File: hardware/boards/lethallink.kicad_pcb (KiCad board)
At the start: 6 copper layers, 86 x 111.1 mm, 125 parts, among them J1 PCIe-x4, J2 USB3_Micro_B_Amphenol, Q1 Q_NMOS_GSD, Q2 Q_NMOS_GSD, Q3 Q_NMOS_GSD, Q4 Q_NMOS_GSD, Q5 SI7232DN-T1-GE3, SW1 SW_DIP_x03, U1 ECP5UM5G-381caBGA, U2 ADP5050ACPZ-R7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

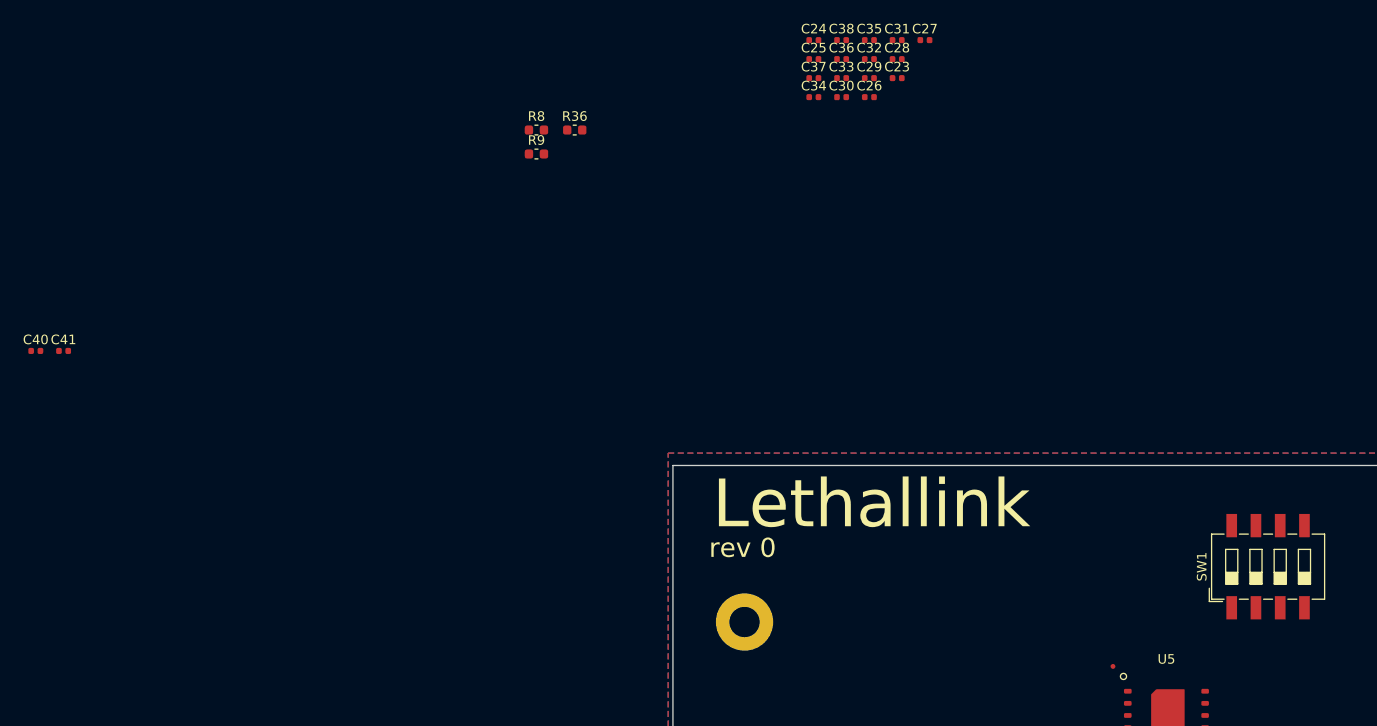
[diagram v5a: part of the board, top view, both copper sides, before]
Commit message: Spent a bit of time putting the unrouted parts back on-grid
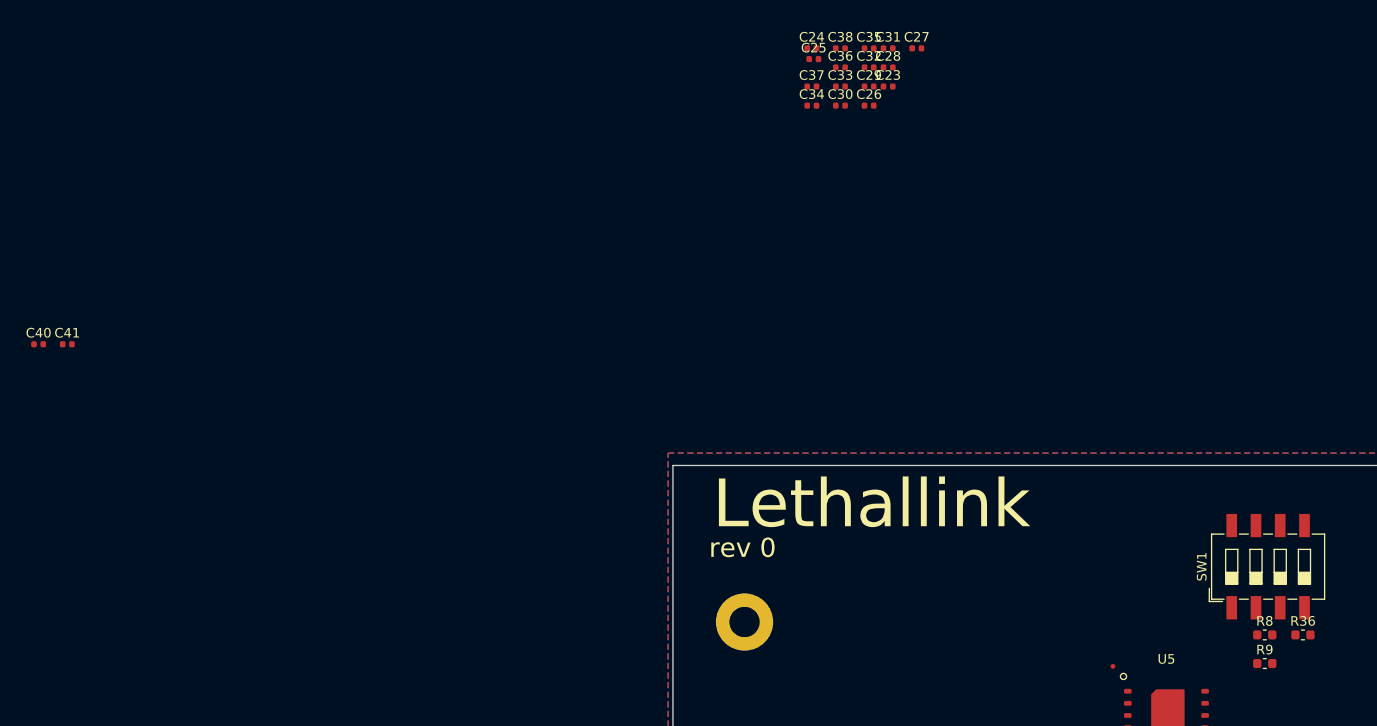
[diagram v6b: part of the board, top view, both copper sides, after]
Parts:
- moved R9 93.1 mm to (79.5, 36.5)
- moved R8 92.8 mm to (79.5, 33.5)
- moved R36 92.8 mm to (83.5, 33.5)
- moved C23 1.29 mm to (40.0, -24.0)
- moved C28 1.28 mm to (40.0, -26.0)
- moved C31 1.27 mm to (40.0, -28.0)
- moved C27 1.21 mm to (43.0, -28.0)
- moved C34 0.91 mm to (32.0, -22.0)
- moved C37 0.90 mm to (32.0, -24.0)
- moved C30 0.90 mm to (35.0, -22.0)
- moved C26 0.89 mm to (38.0, -22.0)
- moved C33 0.89 mm to (35.0, -24.0)
- moved C24 0.89 mm to (32.0, -28.0)
- moved C29 0.88 mm to (38.0, -24.0)
- moved C36 0.88 mm to (35.0, -26.0)
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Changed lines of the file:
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@@
   )
   (module Resistor_SMD:R_0603_1608Metric (layer F.Cu)
-    (at 7.16 -19.44)
+    (at 83.45 33.45)
     (descr "Resistor SMD 0603 (1608 Metric), square (rectangular) end terminal, IPC_7351 nominal, (Body size source: http://www.tortai-tech.com/upload/download/2011102023233369053.pdf), generated with kicad-footprint-generator")
     (tags resistor)
@@
   )
   (module Resistor_SMD:R_0603_1608Metric (layer F.Cu)
-    (at 3.15 -16.93)
+    (at 79.45 36.45)
     (descr "Resistor SMD 0603 (1608 Metric), square (rectangular) end terminal, IPC_7351 nominal, (Body size source: http://www.tortai-tech.com/upload/download/2011102023233369053.pdf), generated with kicad-footprint-generator")
     (tags resistor)
@@
   )
   (module Resistor_SMD:R_0603_1608Metric (layer F.Cu)
-    (at 3.15 -19.44)
+    (at 79.45 33.45)
     (descr "Resistor SMD 0603 (1608 Metric), square (rectangular) end terminal, IPC_7351 nominal, (Body size source: http://www.tortai-tech.com/upload/download/2011102023233369053.pdf), generated with kicad-footprint-generator")
     (tags resistor)
@@
   )
   (module Capacitor_SMD:C_0402_1005Metric (layer F.Cu)
-    (at -46.39 3.7)
+    (at -46 3)
     (descr "Capacitor SMD 0402 (1005 Metric), square (rectangular) end terminal, IPC_7351 nominal, (Body size source: http://www.tortai-tech.com/upload/download/2011102023233369053.pdf), generated with kicad-footprint-generator")
     (tags capacitor)
@@
   )
   (module Capacitor_SMD:C_0402_1005Metric (layer F.Cu)
-    (at -49.3 3.7)
+    (at -49 3)
     (descr "Capacitor SMD 0402 (1005 Metric), square (rectangular) end terminal, IPC_7351 nominal, (Body size source: http://www.tortai-tech.com/upload/download/2011102023233369053.pdf), generated with kicad-footprint-generator")
     (tags capacitor)
@@
   )
   (module Capacitor_SMD:C_0402_1005Metric (layer F.Cu)
-    (at 35.12 -28.86)
+    (at 35 -28)
     (descr "Capacitor SMD 0402 (1005 Metric), square (rectangular) end terminal, IPC_7351 nominal, (Body size source: http://www.tortai-tech.com/upload/download/2011102023233369053.pdf), generated with kicad-footprint-generator")
     (tags capacitor)
@@
   )
   (module Capacitor_SMD:C_0402_1005Metric (layer F.Cu)
-    (at 32.21 -24.88)
+    (at 32 -24)
     (descr "Capacitor SMD 0402 (1005 Metric), square (rectangular) end terminal, IPC_7351 nominal, (Body size source: http://www.tortai-tech.com/upload/download/2011102023233369053.pdf), generated with kicad-footprint-generator")
     (tags capacitor)
@@
   )
   (module Capacitor_SMD:C_0402_1005Metric (layer F.Cu)
-    (at 35.12 -26.87)
+    (at 35 -26)
     (descr "Capacitor SMD 0402 (1005 Metric), square (rectangular) end terminal, IPC_7351 nominal, (Body size source: http://www.tortai-tech.com/upload/download/2011102023233369053.pdf), generated with kicad-footprint-generator")
     (tags capacitor)
@@
   )
   (module Capacitor_SMD:C_0402_1005Metric (layer F.Cu)
-    (at 38.03 -28.86)
+    (at 38 -28)
     (descr "Capacitor SMD 0402 (1005 Metric), square (rectangular) end terminal, IPC_7351 nominal, (Body size source: http://www.tortai-tech.com/upload/download/2011102023233369053.pdf), generated with kicad-footprint-generator")
     (tags capacitor)
@@
   )
   (module Capacitor_SMD:C_0402_1005Metric (layer F.Cu)
-    (at 32.21 -22.89)
+    (at 32 -22)
     (descr "Capacitor SMD 0402 (1005 Metric), square (rectangular) end terminal, IPC_7351 nominal, (Body size source: http://www.tortai-tech.com/upload/download/2011102023233369053.pdf), generated with kicad-footprint-generator")
     (tags capacitor)
@@
   )
   (module Capacitor_SMD:C_0402_1005Metric (layer F.Cu)
-    (at 35.12 -24.88)
+    (at 35 -24)
     (descr "Capacitor SMD 0402 (1005 Metric), square (rectangular) end terminal, IPC_7351 nominal, (Body size source: http://www.tortai-tech.com/upload/download/2011102023233369053.pdf), generated with kicad-footprint-generator")
     (tags capacitor)
@@
   )
   (module Capacitor_SMD:C_0402_1005Metric (layer F.Cu)
-    (at 38.03 -26.87)
+    (at 38 -26)
     (descr "Capacitor SMD 0402 (1005 Metric), square (rectangular) end terminal, IPC_7351 nominal, (Body size source: http://www.tortai-tech.com/upload/download/2011102023233369053.pdf), generated with kicad-footprint-generator")
     (tags capacitor)
@@
   )
   (module Capacitor_SMD:C_0402_1005Metric (layer F.Cu)
-    (at 40.94 -28.86)
+    (at 40 -28)
     (descr "Capacitor SMD 0402 (1005 Metric), square (rectangular) end terminal, IPC_7351 nominal, (Body size source: http://www.tortai-tech.com/upload/download/2011102023233369053.pdf), generated with kicad-footprint-generator")
     (tags capacitor)
@@
   )
   (module Capacitor_SMD:C_0402_1005Metric (layer F.Cu)
-    (at 35.12 -22.89)
+    (at 35 -22)
     (descr "Capacitor SMD 0402 (1005 Metric), square (rectangular) end terminal, IPC_7351 nominal, (Body size source: http://www.tortai-tech.com/upload/download/2011102023233369053.pdf), generated with kicad-footprint-generator")
     (tags capacitor)
@@
   )
   (module Capacitor_SMD:C_0402_1005Metric (layer F.Cu)
-    (at 38.03 -24.88)
+    (at 38 -24)
     (descr "Capacitor SMD 0402 (1005 Metric), square (rectangular) end terminal, IPC_7351 nominal, (Body size source: http://www.tortai-tech.com/upload/download/2011102023233369053.pdf), generated with kicad-footprint-generator")
     (tags capacitor)
@@
   )
   (module Capacitor_SMD:C_0402_1005Metric (layer F.Cu)
-    (at 40.94 -26.87)
+    (at 40 -26)
     (descr "Capacitor SMD 0402 (1005 Metric), square (rectangular) end terminal, IPC_7351 nominal, (Body size source: http://www.tortai-tech.com/upload/download/2011102023233369053.pdf), generated with kicad-footprint-generator")
     (tags capacitor)
@@
   )
   (module Capacitor_SMD:C_0402_1005Metric (layer F.Cu)
-    (at 43.85 -28.86)
+    (at 43 -28)
     (descr "Capacitor SMD 0402 (1005 Metric), square (rectangular) end terminal, IPC_7351 nominal, (Body size source: http://www.tortai-tech.com/upload/download/2011102023233369053.pdf), generated with kicad-footprint-generator")
     (tags capacitor)
@@
   )
   (module Capacitor_SMD:C_0402_1005Metric (layer F.Cu)
-    (at 38.03 -22.89)
+    (at 38 -22)
     (descr "Capacitor SMD 0402 (1005 Metric), square (rectangular) end terminal, IPC_7351 nominal, (Body size source: http://www.tortai-tech.com/upload/download/2011102023233369053.pdf), generated with kicad-footprint-generator")
     (tags capacitor)
@@
   )
   (module Capacitor_SMD:C_0402_1005Metric (layer F.Cu)
-    (at 32.21 -28.86)
+    (at 32 -28)
     (descr "Capacitor SMD 0402 (1005 Metric), square (rectangular) end terminal, IPC_7351 nominal, (Body size source: http://www.tortai-tech.com/upload/download/2011102023233369053.pdf), generated with kicad-footprint-generator")
     (tags capacitor)
@@
   )
   (module Capacitor_SMD:C_0402_1005Metric (layer F.Cu)
-    (at 40.94 -24.88)
+    (at 40 -24)
     (descr "Capacitor SMD 0402 (1005 Metric), square (rectangular) end terminal, IPC_7351 nominal, (Body size source: http://www.tortai-tech.com/upload/download/2011102023233369053.pdf), generated with kicad-footprint-generator")
     (tags capacitor)

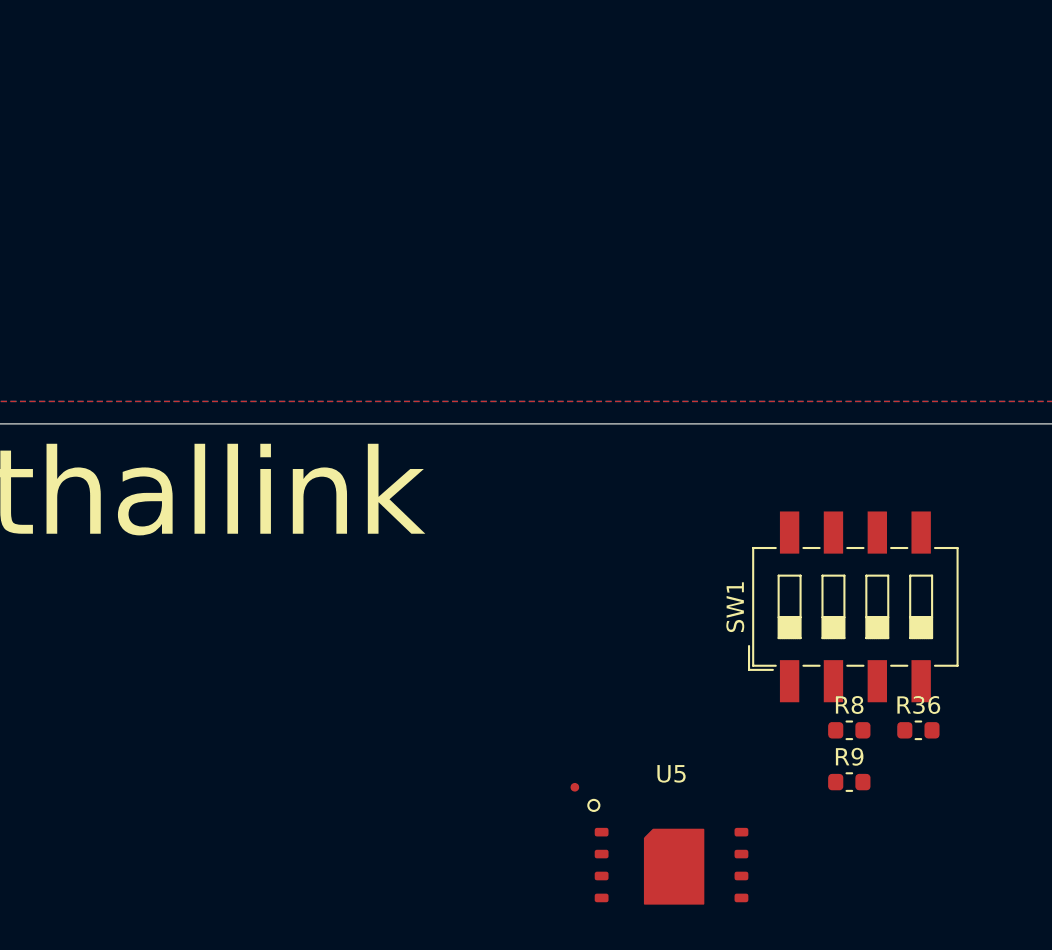
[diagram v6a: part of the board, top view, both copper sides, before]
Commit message: Worked on a bit of the power side for the DDR3 Cache
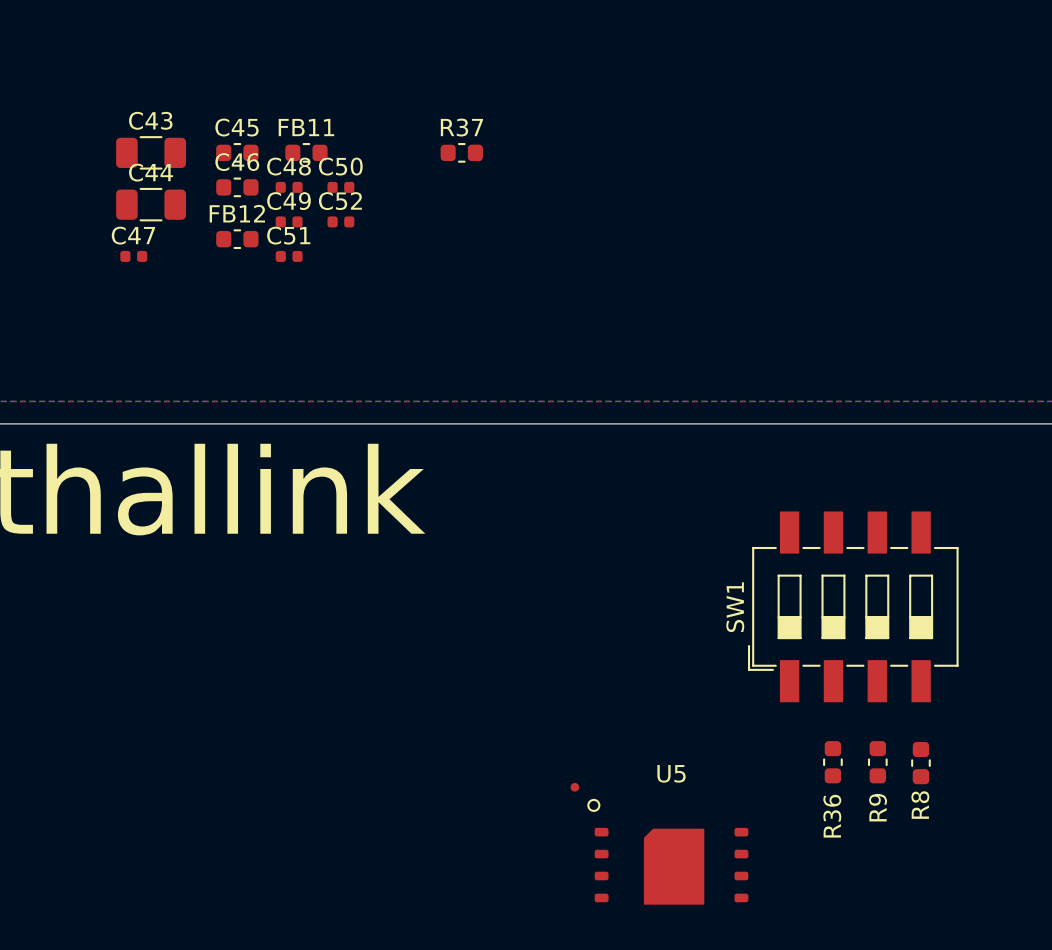
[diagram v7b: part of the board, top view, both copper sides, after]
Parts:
- added C43: 22uF, Capacitor_SMD:C_1206_3216Metric, F.Cu at (39.0, 0.00)
- added C44: 22uF, Capacitor_SMD:C_1206_3216Metric, F.Cu at (39.0, 3.00)
- added C45: 1uF, Capacitor_SMD:C_0603_1608Metric, F.Cu at (44.0, 0.00)
- added C46: 1uF, Capacitor_SMD:C_0603_1608Metric, F.Cu at (44.0, 2.00)
- added C47: 10nF, Capacitor_SMD:C_0402_1005Metric, F.Cu at (38.0, 6.00)
- added C48: 100nF, Capacitor_SMD:C_0402_1005Metric, F.Cu at (47.0, 2.00)
- added C49: 10nF, Capacitor_SMD:C_0402_1005Metric, F.Cu at (47.0, 4.00)
- added C50: 10nF, Capacitor_SMD:C_0402_1005Metric, F.Cu at (50.0, 2.00)
- added C51: 100nF, Capacitor_SMD:C_0402_1005Metric, F.Cu at (47.0, 6.00)
- added C52: 10nF, Capacitor_SMD:C_0402_1005Metric, F.Cu at (50.0, 4.00)
- added FB11: 220 @ 100Mhz, Resistor_SMD:R_0603_1608Metric, F.Cu at (48.0, 0.00)
- added FB12: 220 @ 100Mhz, Resistor_SMD:R_0603_1608Metric, F.Cu at (44.0, 5.00)
- added R37: 240, Resistor_SMD:R_0603_1608Metric, F.Cu at (57.0, 0.00)
- moved R36 5.28 mm to (78.5, 35.3), turned to 90 degrees
- moved R8 4.56 mm to (83.6, 35.4), turned to 90 degrees
- moved R9 2.01 mm to (81.1, 35.3), turned to 90 degrees
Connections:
- U1 pad H6: Net-(U1-PadH6) -> +1V5
- U1 pad H7: Net-(U1-PadH6) -> +1V5
- U1 pad J6: Net-(U1-PadH6) -> +1V5
- U1 pad L6: Net-(U1-PadL6) -> +1V5
- U1 pad L7: Net-(U1-PadL6) -> +1V5
- U1 pad M6: Net-(U1-PadL6) -> +1V5
- U4 pad A9: Net-(U4-PadA9) -> GND
- U4 pad B1: Net-(U4-PadB1) -> GND
- U4 pad B3: Net-(U4-PadA9) -> GND
- U4 pad B9: Net-(U4-PadB1) -> GND
- U4 pad D1: Net-(U4-PadB1) -> GND
- U4 pad D8: Net-(U4-PadB1) -> GND
- U4 pad E1: Net-(U4-PadA9) -> GND
- U4 pad E2: Net-(U4-PadB1) -> GND
- U4 pad E8: Net-(U4-PadB1) -> GND
- U4 pad F9: Net-(U4-PadB1) -> GND
- U4 pad G1: Net-(U4-PadB1) -> GND
- U4 pad G8: Net-(U4-PadA9) -> GND
- U4 pad G9: Net-(U4-PadB1) -> GND
- U4 pad J2: Net-(U4-PadA9) -> GND
- U4 pad J8: Net-(U4-PadA9) -> GND
- U4 pad M1: Net-(U4-PadA9) -> GND
- U4 pad M9: Net-(U4-PadA9) -> GND
- U4 pad P1: Net-(U4-PadA9) -> GND
- U4 pad P9: Net-(U4-PadA9) -> GND
- U4 pad T1: Net-(U4-PadA9) -> GND
- U4 pad T9: Net-(U4-PadA9) -> GND
